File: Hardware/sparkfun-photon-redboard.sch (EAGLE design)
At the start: 54 parts, among them U1 WM-N-BM-14

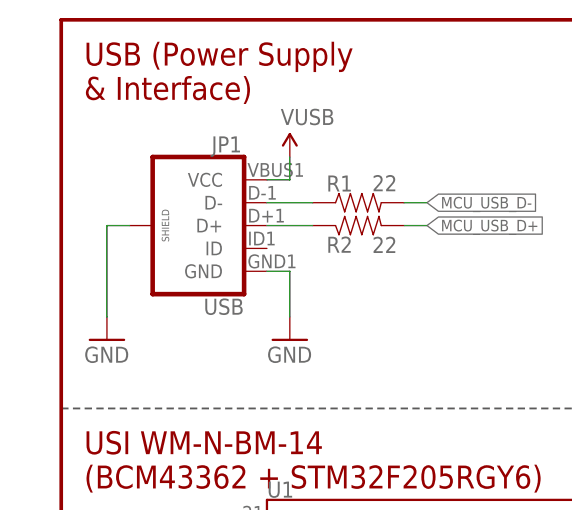
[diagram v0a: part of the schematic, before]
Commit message: Photon Redboard with New USB Connector
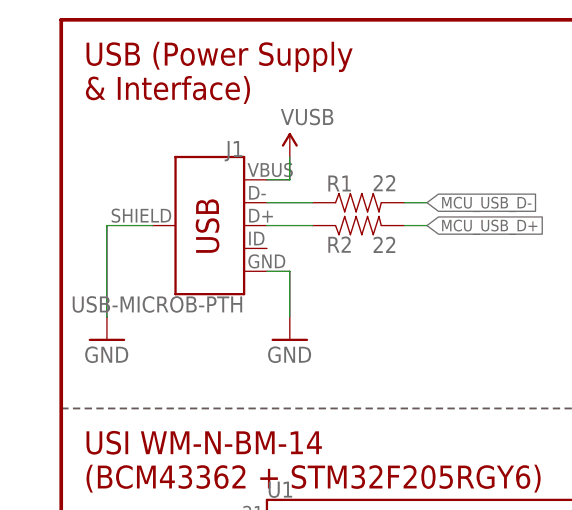
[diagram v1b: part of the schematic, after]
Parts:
- removed JP1: USB, SparkFun-Connectors:USB_MICROB_PLUGCONN-11752
- added J1: USB-MICROB-PTH, SparkFun-Connectors:USB-MICROB-PTH
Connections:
- net D+: now also J1.D+; no longer JP1.D+
- net D-: now also J1.D-; no longer JP1.D-
- net GND: now also J1.GND, J1.SHIELD; no longer JP1.GND, JP1.SHIELD
- net VUSB: now also J1.VBUS; no longer JP1.VCC

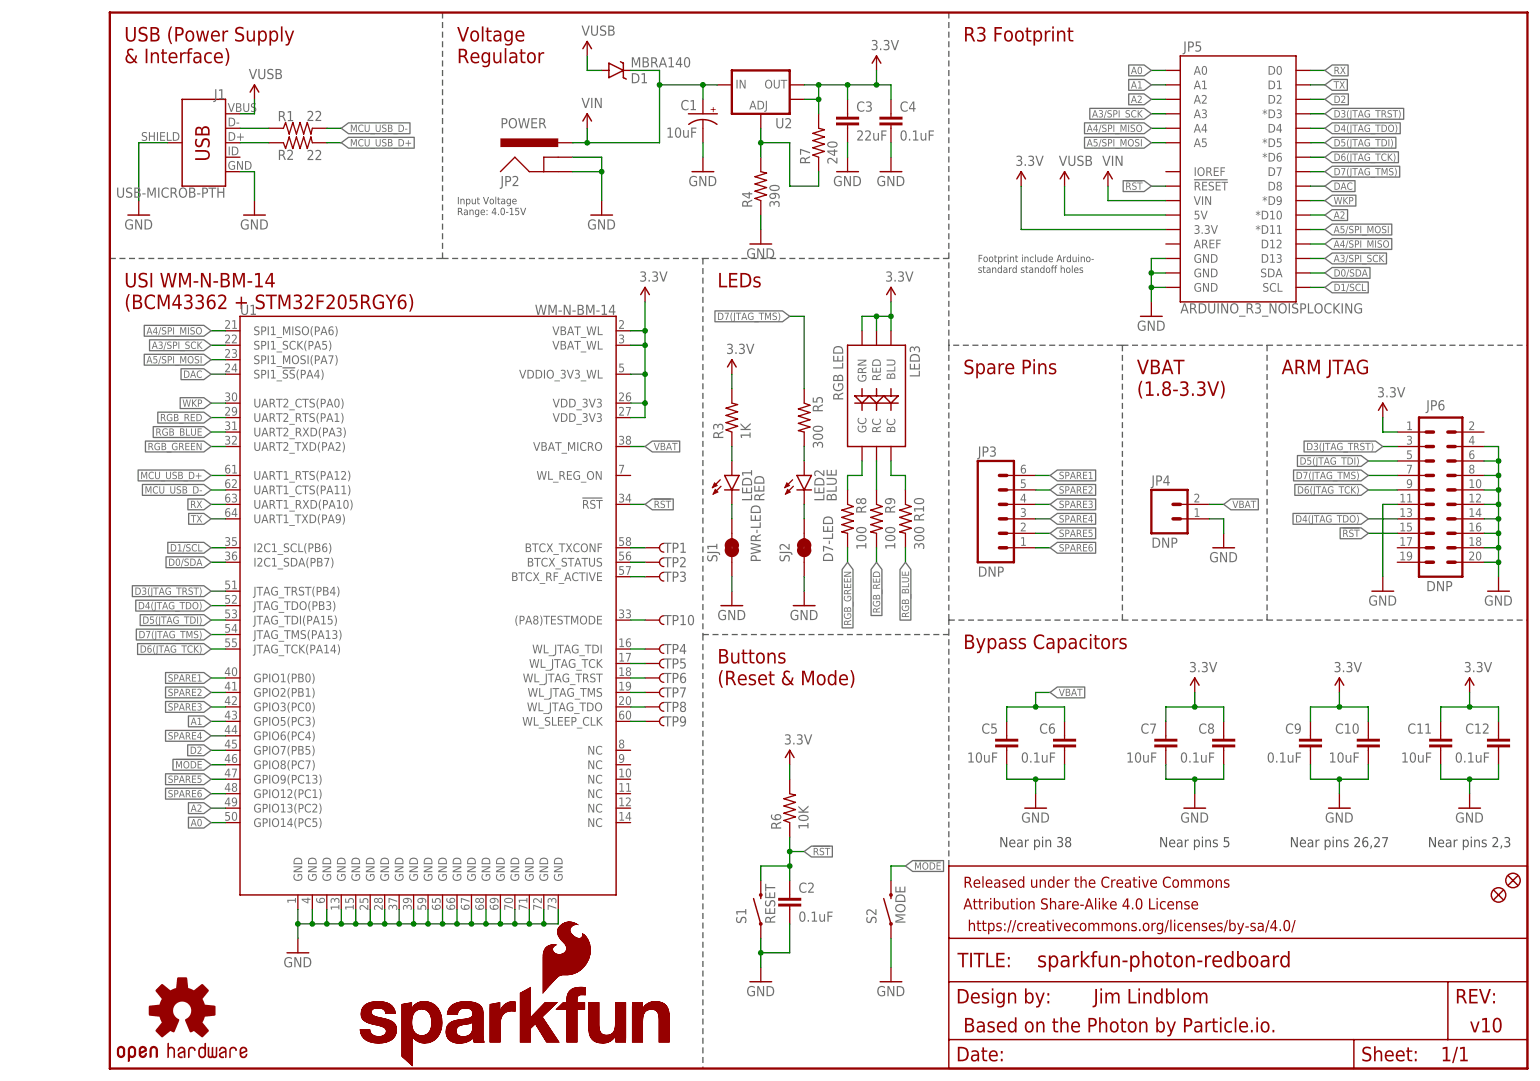
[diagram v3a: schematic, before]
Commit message: Updated RedBoard with new PTH USB
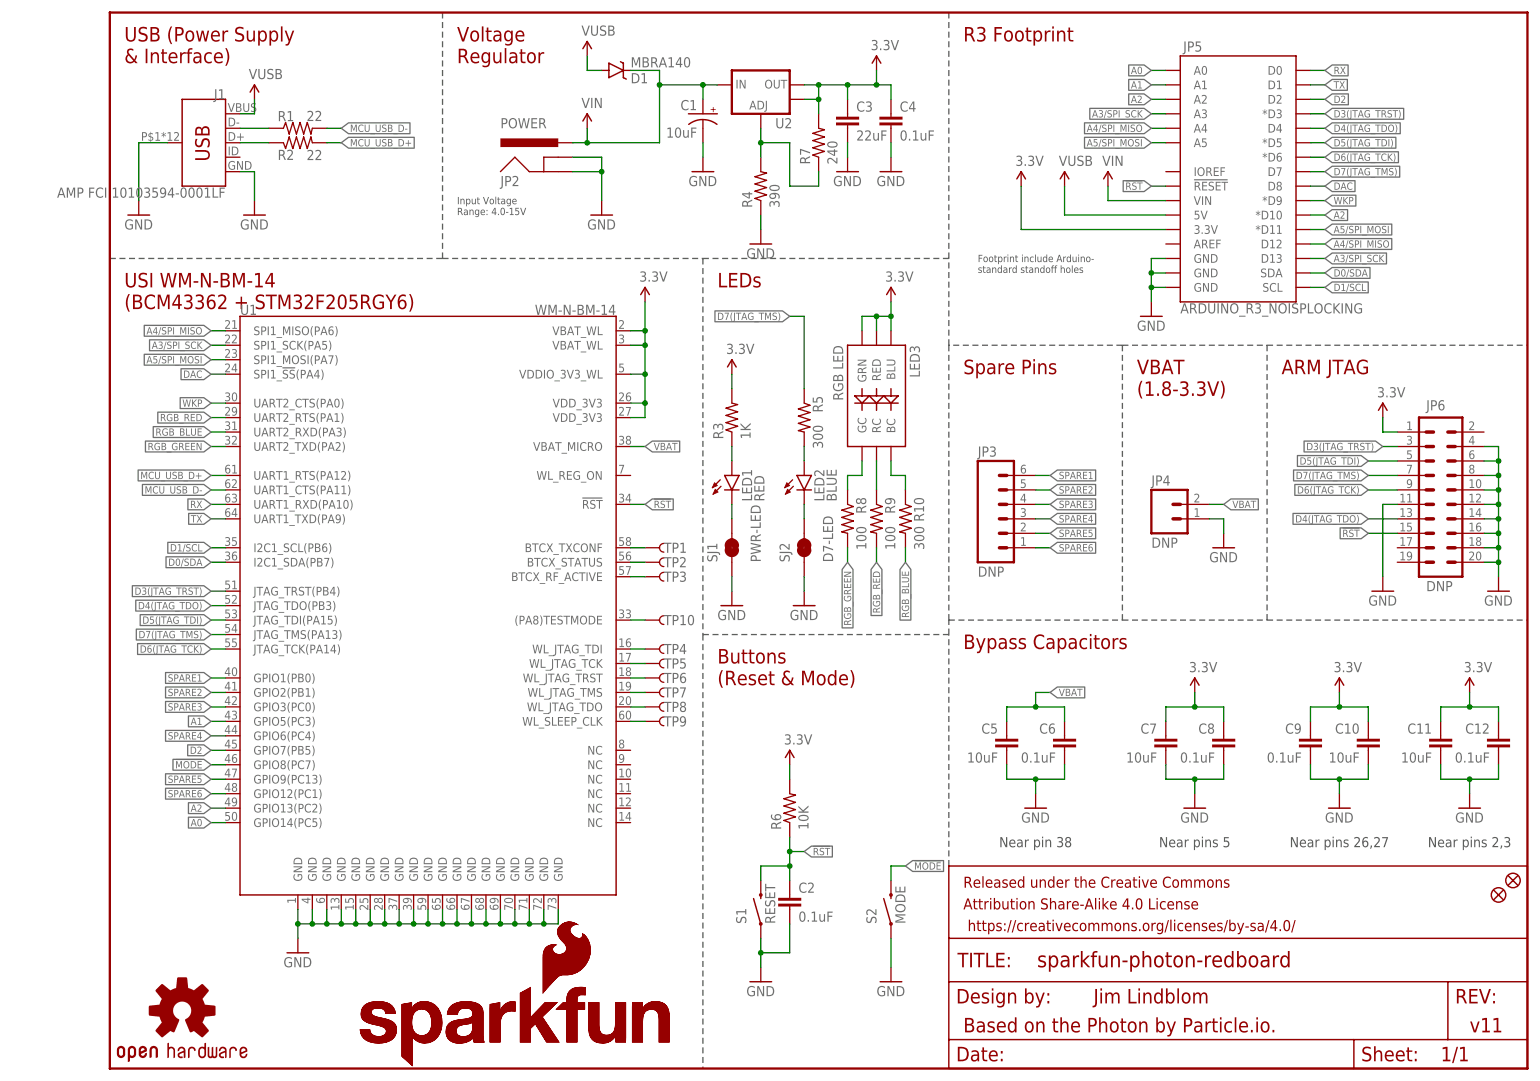
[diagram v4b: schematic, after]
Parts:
- J1: value USB-MICROB-PTH -> AMP FCI 10103594-0001LF; device SparkFun-Connectors:USB-MICROB-PTH -> SparkFun-Connectors:USB_MICRO-B_HALF_PTH
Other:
- note added: "v11"
- note removed: "v10"
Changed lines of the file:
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@@
 <part name="SJ2" library="SparkFun-Passives" deviceset="JUMPER-PAD-2-NC_BY_TRACE" device="" value="D7-LED"/>
 <part name="LOGO3" library="SparkFun-Aesthetics" deviceset="SFE_LOGO_NAME_FLAME" device=".4_INCH" value="SFE_LOGO_NAME_FLAME.4_INCH"/>
-<part name="J1" library="SparkFun-Connectors" deviceset="USB-MICROB-PTH" device=""/>
+<part name="J1" library="SparkFun-Connectors" deviceset="USB_MICRO-B" device="_HALF_PTH" value="AMP FCI 10103594-0001LF"/>
 </parts>
 <sheets>
@@
 <text x="149.86" y="7.62" size="2.54" layer="94" align="center-left">Based on the Photon by Particle.io.</text>
 <text x="172.72" y="12.7" size="2.54" layer="94" align="center-left">Jim Lindblom</text>
-<text x="238.76" y="7.62" size="2.54" layer="94" align="center-left">v10</text>
+<text x="238.76" y="7.62" size="2.54" layer="94" align="center-left">v11</text>
 <text x="60.96" y="149.86" size="1.27" layer="97">Input Voltage
 Range: 4.0-15V</text>
@@
 <instance part="SJ2" gate="G$1" x="121.92" y="91.44" rot="R90"/>
 <instance part="LOGO3" gate="G$1" x="43.18" y="0"/>
-<instance part="J1" gate="&gt;NAME" x="17.78" y="162.56" rot="MR0"/>
+<instance part="J1" gate="G$1" x="17.78" y="162.56" rot="MR0"/>
 </instances>
 <busses>
@@
 <pinref part="GND1" gate="1" pin="GND"/>
 <wire x1="5.08" y1="162.56" x2="5.08" y2="152.4" width="0.1524" layer="91"/>
-<pinref part="J1" gate="&gt;NAME" pin="SHIELD"/>
+<pinref part="J1" gate="G$1" pin="SHIELD"/>
 <wire x1="10.16" y1="162.56" x2="5.08" y2="162.56" width="0.1524" layer="91"/>
 </segment>
@@
 <wire x1="22.86" y1="157.48" x2="25.4" y2="157.48" width="0.1524" layer="91"/>
 <wire x1="25.4" y1="157.48" x2="25.4" y2="152.4" width="0.1524" layer="91"/>
-<pinref part="J1" gate="&gt;NAME" pin="GND"/>
+<pinref part="J1" gate="G$1" pin="GND"/>
 </segment>
 <segment>
@@
 <pinref part="R1" gate="G$1" pin="1"/>
 <wire x1="22.86" y1="165.1" x2="27.94" y2="165.1" width="0.1524" layer="91"/>
-<pinref part="J1" gate="&gt;NAME" pin="D-"/>
+<pinref part="J1" gate="G$1" pin="D-"/>
 </segment>
 </net>
@@
 <pinref part="R2" gate="G$1" pin="1"/>
 <wire x1="22.86" y1="162.56" x2="27.94" y2="162.56" width="0.1524" layer="91"/>
-<pinref part="J1" gate="&gt;NAME" pin="D+"/>
+<pinref part="J1" gate="G$1" pin="D+"/>
 </segment>
 </net>
@@
 <wire x1="25.4" y1="167.64" x2="25.4" y2="170.18" width="0.1524" layer="91"/>
 <pinref part="SUPPLY1" gate="G$1" pin="VUSB"/>
-<pinref part="J1" gate="&gt;NAME" pin="VBUS"/>
-</segment>
-<segment>
+<pinref part="J1" gate="G$1" pin="VBUS"/>
+</segment>
+<segment>
